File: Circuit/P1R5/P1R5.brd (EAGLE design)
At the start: 50.8 x 50.8 mm, 198 parts, among them J1 2X5_0.05"_CORTEX_DEBUGTH_NOKE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, U1 MK20DX256VLH7, U2 TPS61200, U3 PCA9552BS, U4 PCA9552BS, U5 MPU-9250, U6 25Q40, U7 ESP8266EX, U8 NRF24L01, Y1 8MHz, Y2 34.728kHz, Y3 26 Mhz, Y4 16 Mhz

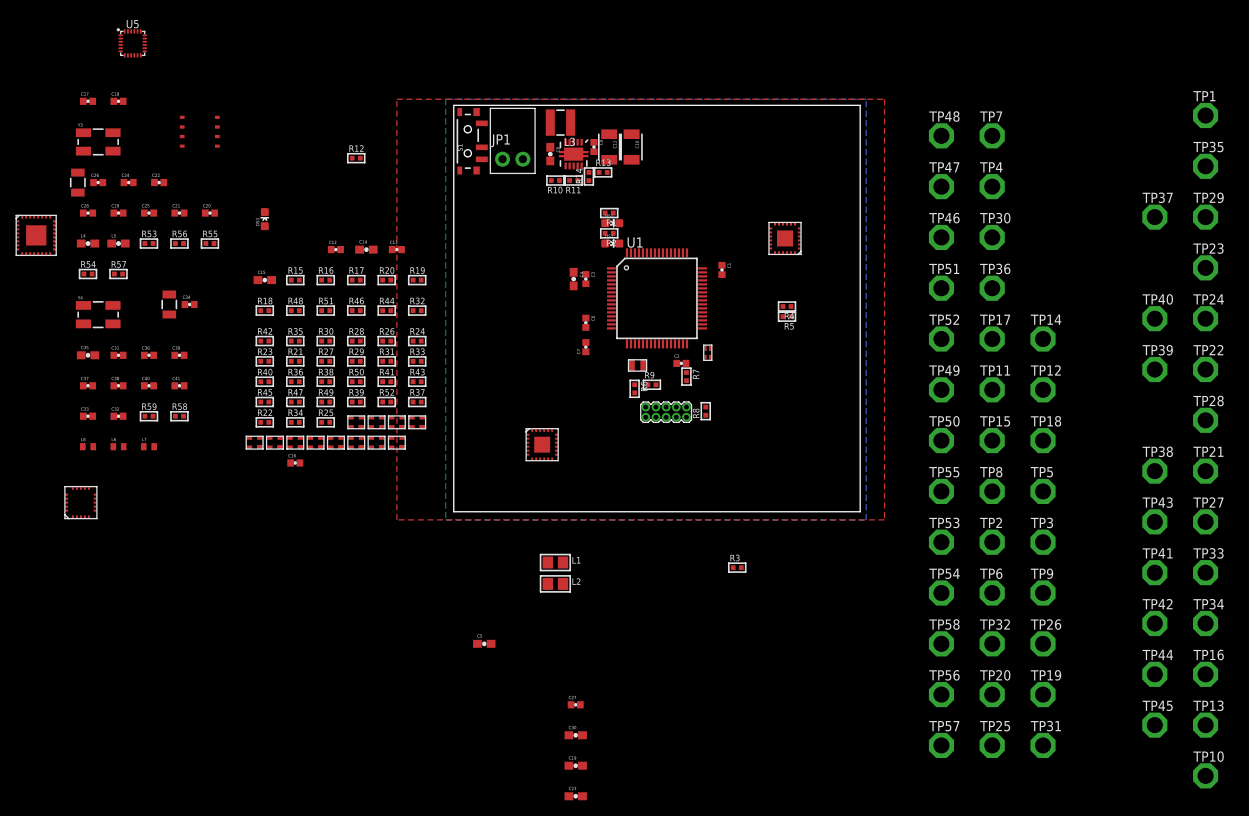
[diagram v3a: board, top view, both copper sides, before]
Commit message: Got majority of PCB layout done.
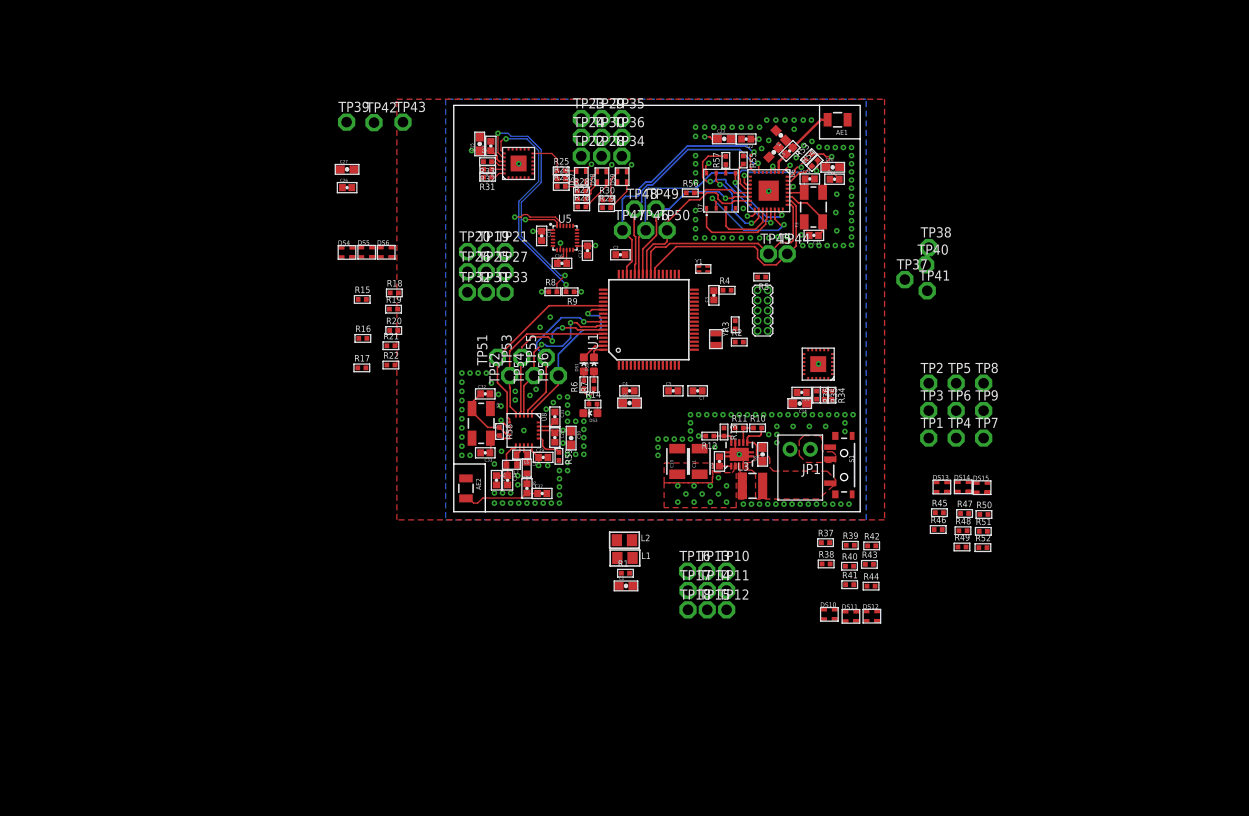
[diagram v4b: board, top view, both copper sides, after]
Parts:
- removed C38: 4.7 pF, SparkFun-Capacitors:0402-CAP
- removed C39: 1.0 pF, SparkFun-Capacitors:0402-CAP
- removed C40, C41: 22 pF, SparkFun-Capacitors:0402-CAP
- removed TP57, TP58: TPPAD1-20, testpad:P1-20
- C1, C6: value 0.1uF -> 10uF; device SparkFun-Capacitors:0402-CAP -> SparkFun-Capacitors:0603-CAP
- C19: value 10uF -> 5.6 pF; device SparkFun-Capacitors:0603-CAP -> SparkFun-Capacitors:0402-CAP
- C20, C27: value 0.1 uF -> 10uF; device SparkFun-Capacitors:0402-CAP -> SparkFun-Capacitors:0603-CAP
- C22: value 15 pF -> 0.1 uF
- C25: value 0.1 uF -> 15 pF
- C26: value 5.6 pF -> 0.1 uF
- C32, C33: value 0.1 uF -> 22 pF
- C34: value 0.1uF -> 2200 pF
- C35: value 10uF -> 4.7 pF; device SparkFun-Capacitors:0603-CAP -> SparkFun-Capacitors:0402-CAP
- C37: value 2200 pF -> 1.0 pF
- C4, C5: value 10uF -> 0.1uF; device SparkFun-Capacitors:0603-CAP -> SparkFun-Capacitors:0402-CAP
- L7: value 3.9 nH -> 2.7 nH
- L8: value 2.7 nH -> 3.9 nH
- R1: value 25 -> 470
- R12: value 25 -> 1.2M
- R13: value 1.2M -> 220K
- R14: value 220K -> 25
- R15, R16, R17, R18, R19, R20: value 10k -> 86.6
- R2: value 25 -> 10k
- R3: value 470 -> 10k
- R31, R32, R33, R34, R35, R36: value 86.6 -> 10k
- R55: value 200 -> 12k
- R56: value 12k -> 10k
- R57: value 10k -> 200
- R58: value 22k -> 1M
- R59: value 1M -> 22k
- R6, R7: value 10k -> 25
- TP1, TP10, TP11, TP12, TP13, TP14, TP15, TP16, TP17, TP18, TP19, TP2, TP20, TP21, TP22, TP23, TP24, TP25, TP26, TP27, TP28, TP29, TP3, TP30, TP31, TP32, TP33, TP34, TP35, TP36, TP37, TP38, TP39, TP4, TP40, TP41, TP42, TP43, TP44, TP45, TP46, TP47, TP48, TP49, TP5, TP50, TP51, TP52, TP53, TP54, TP55, TP56, TP6, TP7, TP8, TP9: value TPPAD1-20 -> TPPAD1-13; device testpad:P1-20 -> testpad:P1-13
- U6: value 25Q40 -> ESP8266EX; device wifi:SOP8 -> wifi:QFN32
- U7: value ESP8266EX -> 25Q40; device wifi:QFN32 -> wifi:SOP8
- moved TP42 116.0 mm to (-9.97, 48.6)
- moved TP43 106.4 mm to (-6.35, 48.7)
- moved TP39 105.7 mm to (-13.4, 48.7)
- moved AE1 95.3 mm to (48.0, 49.0), turned to 90 degrees
- moved TP33 94.3 mm to (6.41, 27.4)
- moved TP34 93.5 mm to (21.0, 44.5)
- moved TP27 93.0 mm to (6.41, 30.0)
- moved R54 91.9 mm to (45.1, 43.6), turned to 45 degrees
- moved TP21 91.8 mm to (6.41, 32.5)
- moved Y3 89.8 mm to (45.0, 38.1), turned to 90 degrees
- moved TP31 89.7 mm to (4.08, 27.4)
- moved TP19 88.9 mm to (4.06, 32.5)
- moved R48 87.9 mm to (63.7, -2.37)
- moved L4 87.7 mm to (40.9, 47.0), turned to 135 degrees
- moved R51 86.7 mm to (66.2, -2.45)
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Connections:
- removed net N$118: C29.2, U7.VDD3P3/4, U7.VDD_RTC/5
- removed net N$61 (its old number): DS7.G, R31.2
- new net N$59: DS13.G, R46.2
- net !CS: now also TP42.TP; no longer TP44.TP
- net !RESET0: now also TP37.TP; no longer TP39.TP
- net !RESET1: now also TP38.TP; no longer TP40.TP
- net 3.3V: now also C17.2, C18.1, C21.2, C22.1, C26.2, C27.1, C28.1, C29.1, C6.1, R12.2, R14.1, R36.2, R53.2, R9.1, U6.1, U6.11, U6.17, U6.29, U6.3, U6.30, U6.4, U7.8; no longer C1.1, C16.2, C17.1, C19.1, C21.1, C25.2, C27.2, C28.2, C32.1, C33.1, C34.1, C35.1, R1.1, R12.1, R13.2, R20.2, R54.2, U6.8, U7.VDD3P3/3, U7.VDDA/1, U7.VDDA/30, U7.VDDD/29, U7.VDDPST/11, U7.VDDPST/17
- net CE: now also TP56.TP; no longer TP58.TP
- net CHIP_EN: now also TP48.TP, U6.7; no longer TP50.TP, U7.CHIP_EN/7
- net CLK: now also R57.1, U7.6; no longer R55.1, U6.6
- net CS: now also U6.20, U7.1; no longer U6.1, U7.SD_CMD/20
- net CSN: now also TP55.TP, U1.57; no longer TP57.TP, U1.49
- net DIO: now also U6.23, U7.5; no longer U6.5, U7.SD_DATA_1/23
- net DO: now also U6.22, U7.2; no longer U6.2, U7.SD_DATA_0/22
- net FSYNC: now also TP39.TP; no longer TP41.TP
- net GND: now also C17.1, C18.2, C21.1, C25.2, C26.1, C27.2, C28.2, C29.2, C6.2, R13.1, R3.1, R31.2, R32.2, R33.2, R34.2, R35.2, R54.2, R55.1, R59.2, U6.PAD, U7.4; no longer C1.2, C17.2, C18.1, C19.2, C21.2, C25.1, C27.1, C28.1, C29.1, C38.2, C39.2, C40.2, C41.2, R14.1, R15.2, R16.2, R17.2, R18.2, R19.2, R53.2, R57.1, R58.2, R9.1, U6.4, U7.GND
- net GPIO0: now also TP50.TP, U6.15; no longer TP52.TP, U7.GPIO0/15
- net GPIO2: now also TP49.TP, U6.14; no longer TP51.TP, U7.GPIO2/14
- net HOLD#: now also U6.18, U7.7; no longer U6.7, U7.SD_DATA_2/18
- net INT: now also TP43.TP; no longer TP45.TP
- net IRQ: now also TP51.TP; no longer TP53.TP
- net MISO: now also TP52.TP, U1.60; no longer TP54.TP, U1.52
- net MOSI: now also TP53.TP, U1.59; no longer TP55.TP, U1.51
- net N$100: now also C24.1, U6.28; no longer C22.1, U7.XTAL_IN/28
- net N$101: now also C19.1; no longer C26.1
- net N$102: now also R55.2, U6.12; no longer R56.2, U7.MTCK/12
- net N$103: now also R56.2, U6.13; no longer R57.2, U7.MTDO/13
- net N$107: now also R54.1, U6.31; no longer R53.1, U7.RES12K/31
- net N$108: now also C32.1, R58.1; no longer C40.1, R59.1
- net N$109: now also C33.1, R58.2; no longer C41.1, R59.2
- net N$11: now also U1.50; no longer U1.58
- net N$111: now also L8.1; no longer L7.1
- net N$112: now also R59.1; no longer R58.1
- net N$114: now also L7.1; no longer L8.1
- net N$115: now also C37.1; no longer C39.1
- net N$116: now also L8.2; no longer L7.2
- net N$117: now also C34.1, C35.1, L7.2; no longer C37.1, C38.1, L8.2
- net N$15: now also U1.49; no longer U1.57
- net N$22: now also C19.2, U6.2; no longer C26.2, U7.LNA/2
- net N$23: now also C25.1, U6.27; no longer C24.1, U7.XTAL_OUT/27
- net N$27: now also R12.1, R13.2; no longer R13.1, R14.2
- net N$28: now also R14.2; no longer R12.2
- net N$29: now also R7.2; no longer R2.2
- net N$3: now also R57.2, U6.21; no longer R55.2, U7.SD_CLK/21
- net N$30: now also R32.1; no longer R16.1
- net N$31: now also R33.1; no longer R17.1
- net N$32: now also R34.1; no longer R18.1
- net N$33: now also R35.1; no longer R19.1
- net N$34: now also R36.1; no longer R20.1
- net N$35: now also R31.1; no longer R15.1
- net N$36: now also DS8.R, R27.2; no longer DS12.R, R44.2
- net N$37: now also DS7.R, R24.2; no longer DS10.R, R39.2
- net N$38: now also DS7.B, R25.2; no longer DS10.B, R40.2
- net N$39: now also DS7.G, R23.2; no longer DS10.G, R37.2
- net N$4: now also C16.2; no longer C18.2
- net N$40: now also DS8.B, R28.2; no longer DS12.B, R46.2
- net N$41: now also DS8.G, R26.2; no longer DS12.G, R42.2
- net N$42: now also DS10.G, R38.2; no longer DS5.G, R25.2
- net N$43: now also DS10.B, R37.2; no longer DS5.B, R22.2
- net N$44: now also DS9.B, R30.2; no longer DS14.B, R51.2
- net N$45: now also DS9.G, R29.2; no longer DS14.G, R48.2
- net N$46: now also R15.1; no longer R21.1
- net N$47: now also DS5.R, R19.2; no longer DS6.R, R28.2
- net N$48: now also R16.1; no longer R23.1
- net N$49: now also R17.1; no longer R24.1
- net N$5: now also U1.52; no longer U1.60
- net N$50: now also DS14.B, R47.2; no longer DS13.B, R43.2
- net N$51: now also R16.2; no longer R23.2
- net N$52: now also DS11.R, R40.2; no longer DS7.R, R29.2
- net N$53: now also R17.2; no longer R24.2
- net N$54: now also R15.2; no longer R21.2
- net N$55: now also DS5.B, R20.2; no longer DS6.B, R30.2
- net N$56: now also DS5.G, R18.2; no longer DS6.G, R26.2
- net N$58: now also DS12.B, R42.2; no longer DS9.B, R33.2
- net N$6: now also U1.51; no longer U1.59
- net N$60: now also R18.1; no longer R26.1
- net N$62: now also DS14.G, R49.2; no longer DS13.G, R47.2
- net N$63: now also DS11.B, R39.2; no longer DS7.B, R27.2
- net N$64: now also DS12.G, R44.2; no longer DS9.G, R36.2
- net N$65: now also DS6.B, R22.2; no longer DS8.B, R35.2
- net N$66: now also DS6.G, R21.2; no longer DS8.G, R32.2
- net N$67: now also DS14.R, R48.2; no longer DS13.R, R45.2
- net N$68: now also DS13.B, R45.2; no longer DS11.B, R38.2
- net N$69: now also R19.1; no longer R28.1
- net N$7: now also R6.2; no longer R1.2
- net N$70: now also R50.2; no longer R49.2
- net N$71: now also R20.1; no longer R30.1
- net N$72: now also R21.1; no longer R32.1
- net N$73: now also R22.1; no longer R35.1
- net N$74: now also R23.1; no longer R37.1
- net N$75: now also R24.1; no longer R39.1
- net N$76: now also R25.1; no longer R40.1
- net N$77: now also R26.1; no longer R42.1
- net N$78: now also R27.1; no longer R44.1
- net N$79: now also R28.1; no longer R46.1
- net N$80: now also R29.1; no longer R48.1
- net N$81: now also R30.1; no longer R51.1
- net N$82: now also DS12.R, R43.2; no longer DS9.R, R34.2
- net N$83: now also R51.2; no longer R50.2
- net N$84: now also R37.1; no longer R22.1
- net N$85: now also R38.1; no longer R25.1
- net N$86: now also R39.1; no longer R27.1
- net N$87: now also R40.1; no longer R29.1
- net N$88: now also R41.1; no longer R31.1
- net N$89: now also R42.1; no longer R33.1
- net N$90: now also R43.1; no longer R34.1
- net N$91: now also R44.1; no longer R36.1
- net N$92: now also R45.1; no longer R38.1
- net N$93: now also R46.1; no longer R41.1
- net N$94: now also R47.1; no longer R43.1
- net N$95: now also R48.1; no longer R45.1
- net N$96: now also R49.1; no longer R47.1
- net N$97: now also R50.1; no longer R49.1
- net N$98: now also R51.1; no longer R50.1
- net PTA0: now also R3.2; no longer R9.2
- net PTA1: now also R4.2; no longer R7.2
- net PTA3: now also R2.2; no longer R6.2
- net RESET_B: now also R5.2; no longer R8.2
- net SCK: now also TP54.TP, U1.58; no longer TP56.TP, U1.50
- net SCL: now also R9.2, TP40.TP; no longer R5.2, TP42.TP
- net SDA: now also R8.2, TP41.TP; no longer R4.2, TP37.TP, TP38.TP, TP43.TP
- net U0RX: now also TP45.TP, U6.25; no longer TP47.TP, U7.U0RXD/25
- net U0TX: now also TP44.TP, U6.26; no longer TP46.TP, U7.U0TXD/26
- net VDDA: now also C1.1, R1.1; no longer C5.1, R3.1
- net VREFH: now also C5.1, R1.2; no longer C6.1, R3.2
- net VREFL: now also C1.2; no longer C6.2
- net WIFI_RESET: now also R53.1, TP46.TP, U6.32; no longer R54.1, TP48.TP, U7.EXT_RSTB/32
- net WP#: now also U6.19, U7.3; no longer U6.3, U7.SD_DATA_3/19
- net XPD_DCDC: now also TP47.TP, U6.8; no longer TP49.TP, U7.XPD_DCDC/8
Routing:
- net 3.3V: track 0.00 -> 47.5 mm, vias 0 -> 35
- net SDA: track 0.00 -> 36.6 mm, vias 0 -> 3
- net WIFI_RESET: track 0.00 -> 35.7 mm, vias 0 -> 1
- net SCL: track 0.00 -> 35.4 mm, vias 0 -> 3
- net XPD_DCDC: track 0.00 -> 33.1 mm, vias 0 -> 1
- net CHIP_EN: track 0.00 -> 29.5 mm, vias 0 -> 1
- net U0TX: track 0.00 -> 28.5 mm
- net U0RX: track 0.00 -> 27.3 mm
- net IRQ: track 0.00 -> 24.7 mm
- net GPIO2: track 0.00 -> 22.0 mm, vias 0 -> 1
- net GPIO0: track 0.00 -> 21.3 mm
- net CE: track 0.00 -> 21.1 mm, vias 0 -> 1
- net MISO: track 0.00 -> 21.0 mm
- net MOSI: track 0.00 -> 21.0 mm, vias 0 -> 2
- net CSN: track 0.00 -> 20.5 mm, vias 0 -> 1
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- added copper zone on layer 1, net 3.3V
- added copper zone on layer 1, net N$104
- added copper zone on layer 1, net N$24
- added copper zone on layer 1, net V_IN
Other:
- outline, holes or cut-outs redrawn

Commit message: More work on PCB.
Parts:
- removed C15: 10uF, SparkFun-Capacitors:0603-CAP
- removed C16: 0.1 uF, SparkFun-Capacitors:0402-CAP
- removed C37: 1.0 pF, SparkFun-Capacitors:0402-CAP
- removed R30: 86.6, appfruits:_0402
- removed R31, R32, R33, R34, R35: 10k, appfruits:_0402
- removed R59: 22k, appfruits:_0402
- C10: value 22uF -> 0.1uF; device SparkFun-Capacitors:1210 -> SparkFun-Capacitors:0402-CAP
- C12: value 0.1uF -> 22uF; device SparkFun-Capacitors:0402-CAP -> SparkFun-Capacitors:1210
- C14, C6, C8: value 10uF -> 0.1uF; device SparkFun-Capacitors:0603-CAP -> SparkFun-Capacitors:0402-CAP
- C19: value 5.6 pF -> 0.1 uF
- C20: value 10uF -> 5.6 pF; device SparkFun-Capacitors:0603-CAP -> SparkFun-Capacitors:0402-CAP
- C21, C29: value 0.1 uF -> 10uF; device SparkFun-Capacitors:0402-CAP -> SparkFun-Capacitors:0603-CAP
- C23, C27: value 10uF -> 0.1 uF; device SparkFun-Capacitors:0603-CAP -> SparkFun-Capacitors:0402-CAP
- C24: value 15 pF -> 10uF; device SparkFun-Capacitors:0402-CAP -> SparkFun-Capacitors:0603-CAP
- C26: value 0.1 uF -> 15 pF
- C30: value 10uF -> .033 uF; device SparkFun-Capacitors:0603-CAP -> SparkFun-Capacitors:0402-CAP
- C31: value .033 uF -> 22 pF
- C33: value 22 pF -> 2200 pF
- C34: value 2200 pF -> 4.7 pF
- C35: value 4.7 pF -> 1.5 pF
- C36: value 1.5 pF -> 1.0 pF
- C4, C7, C9: value 0.1uF -> 10uF; device SparkFun-Capacitors:0402-CAP -> SparkFun-Capacitors:0603-CAP
- R1: value 470 -> 10k
- R10: value 2M -> 220K
- R11: value 220K -> 1.2M
- R12: value 1.2M -> 220K
- R13: value 220K -> 25
- R14: value 25 -> 86.6
- R36: value 10k -> 86.6
- R5: value 10k -> 25
- R52: value 86.6 -> 12k
- R55: value 12k -> 10k
- R56: value 10k -> 200
- R57: value 200 -> 1M
- R58: value 1M -> 22k
- R7: value 25 -> 10k
- R9: value 10k -> 2M
- TP37, TP38, TP39, TP40, TP42, TP43, TP44, TP45, TP46, TP47, TP48, TP49, TP50, TP51, TP52, TP53, TP54, TP55, TP56: value TPPAD1-13 -> TPTP08R; device testpad:P1-13 -> testpad:TP08R
- moved TP41 65.1 mm to (-4.70, 40.4)
- moved TP6 63.9 mm to (1.65, 31.1)
- moved TP4 63.4 mm to (1.65, 26.0)
- moved TP5 62.4 mm to (1.65, 28.5)
- moved TP15 62.3 mm to (21.0, 49.1)
- moved TP9 62.3 mm to (6.73, 31.1)
- moved TP7 61.8 mm to (6.73, 26.0)
- moved TP8 60.8 mm to (6.73, 28.5)
- moved TP14 60.5 mm to (18.5, 49.1)
- moved TP18 59.6 mm to (21.0, 46.8)
- moved TP38 59.2 mm to (1.63, 45.9)
- moved TP13 58.7 mm to (15.9, 49.1)
- moved C26 58.6 mm to (45.0, 34.5), turned to 180 degrees
- moved TP12 58.2 mm to (21.0, 44.5)
- moved TP3 58.2 mm to (4.19, 31.1)
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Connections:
- removed net N$30: R32.1, U3.23
- removed net N$31: R33.1, U3.22
- removed net N$32: R34.1, U4.24
- removed net N$33: R35.1, U4.23
- removed net N$34: R36.1, U4.22
- removed net N$35: R31.1, U3.24
- removed net VREFH: C5.1, R1.2, U1.14
- removed net VREFL: C1.2, C5.2, C7.2, L2.2, U1.15, U1.16
- new net AGND: C4.2, C6.2, C8.2, L2.2, U1.15, U1.16
- net !RESET0: now also TP39.TP; no longer TP37.TP
- net !RESET1: now also TP40.TP; no longer TP38.TP
- net 3.3V: now also C1.1, C18.2, C19.1, C21.1, C22.2, C24.1, C5.1, C7.1, R1.1, R11.2, R13.1, R3.1, R52.2, TP1.TP, TP16.TP, TP17.TP, TP2.TP, TP32.TP, TP33.TP, TP34.TP, TP35.TP, U4.22; no longer C10.1, C15.1, C17.2, C18.1, C20.1, C21.2, C22.1, C26.2, C30.1, C4.1, C6.1, R12.2, R14.1, R2.1, R36.2, R53.2, R9.1, TP12.TP, TP15.TP, TP19.TP, TP24.TP, TP25.TP, TP30.TP, TP6.TP, TP9.TP
- net CHIP_EN: now also TP46.TP; no longer TP48.TP
- net CLK: now also R56.1; no longer R57.1
- net FSYNC: now also TP41.TP; no longer TP39.TP
- net GND: now also C1.2, C18.1, C19.2, C21.2, C22.1, C26.2, C30.1, C31.2, C36.2, C5.2, C7.2, R10.1, R12.1, R2.1, R53.2, R54.1, R58.2, TP13.TP, TP15.TP, TP25.TP, TP27.TP, TP28.TP, TP30.TP, TP4.TP, TP6.TP, U3.22, U3.23, U3.24, U4.23, U4.24; no longer C15.2, C16.1, C18.2, C20.2, C21.1, C22.2, C26.1, C30.2, C31.1, C35.2, C37.2, C4.2, C6.2, C8.2, R11.1, R13.1, R3.1, R31.2, R32.2, R33.2, R34.2, R35.2, R54.2, R56.1, R59.2, TP11.TP, TP17.TP, TP2.TP, TP20.TP, TP23.TP, TP32.TP, TP35.TP, TP8.TP
- net GPIO0: now also TP49.TP; no longer TP50.TP
- net GPIO2: now also TP47.TP; no longer TP49.TP
- net N$100: now also C25.1; no longer C24.1
- net N$101: now also C20.1; no longer C19.1
- net N$102: now also R54.2; no longer R55.2
- net N$103: now also R55.2; no longer R56.2
- net N$107: now also R53.1; no longer R54.1
- net N$108: now also C31.1, R57.1; no longer C32.1, R58.1
- net N$109: now also C32.1, R57.2; no longer C33.1, R58.2
- net N$11: now also TP9.TP; no longer TP33.TP
- net N$112: now also R58.1; no longer R59.1
- net N$113: now also C30.2; no longer C31.2
- net N$115: now also C35.2, C36.1; no longer C36.2, C37.1
- net N$116: now also C35.1; no longer C36.1
- net N$117: now also C33.1; no longer C35.1
- net N$12: now also TP10.TP; no longer TP22.TP
- net N$14: now also TP11.TP; no longer TP28.TP
- net N$15: now also TP12.TP; no longer TP34.TP
- net N$16: now also TP24.TP; no longer TP16.TP
- net N$17: now also TP21.TP; no longer TP7.TP
- net N$18: now also TP22.TP; no longer TP10.TP
- net N$19: now also TP23.TP; no longer TP13.TP
- net N$20: now also TP20.TP; no longer TP4.TP
- net N$21: now also TP19.TP; no longer TP1.TP
- net N$22: now also C20.2; no longer C19.2
- net N$23: now also C26.1; no longer C25.1
- net N$25: now also C10.1; no longer C9.1
- net N$26: now also R10.2, R9.1; no longer R10.1, R11.2
- net N$27: now also R11.1, R12.2; no longer R12.1, R13.2
- net N$28: now also R13.2; no longer R14.2
- net N$29: now also R6.2; no longer R7.2
- net N$3: now also R56.2; no longer R57.2
- net N$36: now also R26.2; no longer R27.2
- net N$37: now also R23.2; no longer R24.2
- net N$38: now also R24.2; no longer R25.2
- net N$39: now also R22.2; no longer R23.2
- net N$4: now also C17.2; no longer C16.2
- net N$40: now also R27.2; no longer R28.2
- net N$41: now also R25.2; no longer R26.2
- net N$42: now also R37.2; no longer R38.2
- net N$43: now also R36.2; no longer R37.2
- net N$44: now also R29.2; no longer R30.2
- net N$45: now also R28.2; no longer R29.2
- net N$46: now also R14.1; no longer R15.1
- net N$47: now also R18.2; no longer R19.2
- net N$48: now also R15.1; no longer R16.1
- net N$49: now also R16.1; no longer R17.1
- net N$5: now also TP7.TP; no longer TP21.TP
- net N$50: now also R46.2; no longer R47.2
- net N$51: now also R15.2; no longer R16.2
- net N$52: now also R39.2; no longer R40.2
- net N$53: now also R16.2; no longer R17.2
- net N$54: now also R14.2; no longer R15.2
- net N$55: now also R19.2; no longer R20.2
- net N$56: now also R17.2; no longer R18.2
- net N$57: now also R51.2; no longer R52.2
- net N$58: now also R41.2; no longer R42.2
- net N$59: now also R45.2; no longer R46.2
- net N$6: now also TP8.TP; no longer TP27.TP
- net N$60: now also R17.1; no longer R18.1
- net N$61: now also R40.2; no longer R41.2
- net N$62: now also R48.2; no longer R49.2
- net N$63: now also R38.2; no longer R39.2
- net N$64: now also R43.2; no longer R44.2
- net N$65: now also R21.2; no longer R22.2
- net N$66: now also R20.2; no longer R21.2
- net N$67: now also R47.2; no longer R48.2
- net N$68: now also R44.2; no longer R45.2
- net N$69: now also R18.1; no longer R19.1
- net N$7: now also R5.2; no longer R6.2
- net N$70: now also R49.2; no longer R50.2
- net N$71: now also R19.1; no longer R20.1
- net N$72: now also R20.1; no longer R21.1
- net N$73: now also R21.1; no longer R22.1
- net N$74: now also R22.1; no longer R23.1
- net N$75: now also R23.1; no longer R24.1
- net N$76: now also R24.1; no longer R25.1
- net N$77: now also R25.1; no longer R26.1
- net N$78: now also R26.1; no longer R27.1
- net N$79: now also R27.1; no longer R28.1
- net N$80: now also R28.1; no longer R29.1
- net N$81: now also R29.1; no longer R30.1
- net N$82: now also R42.2; no longer R43.2
- net N$83: now also R50.2; no longer R51.2
- net N$84: now also R36.1; no longer R37.1
- net N$85: now also R37.1; no longer R38.1
- net N$86: now also R38.1; no longer R39.1
- net N$87: now also R39.1; no longer R40.1
- net N$88: now also R40.1; no longer R41.1
- net N$89: now also R41.1; no longer R42.1
- net N$90: now also R42.1; no longer R43.1
- net N$91: now also R43.1; no longer R44.1
- net N$92: now also R44.1; no longer R45.1
- net N$93: now also R45.1; no longer R46.1
- net N$94: now also R46.1; no longer R47.1
- net N$95: now also R47.1; no longer R48.1
- net N$96: now also R48.1; no longer R49.1
- net N$97: now also R49.1; no longer R50.1
- net N$98: now also R50.1; no longer R51.1
- net N$99: now also R51.1; no longer R52.1
- net PTA0: now also R2.2; no longer R3.2
- net PTA1: now also R3.2; no longer R4.2
- net PTA3: now also R1.2; no longer R2.2
- net RESET_B: now also R4.2; no longer R5.2
- net SCL: now also R8.2, TP38.TP; no longer R9.2, TP40.TP
- net SDA: now also R7.2, TP37.TP; no longer R8.2, TP41.TP
- net U0RX: now also TP50.TP; no longer TP45.TP
- net U0TX: now also TP48.TP; no longer TP44.TP
- net VDDA: now also C4.1, C6.1, U1.14; no longer C1.1, R1.1
- net VREF_OUT: now also C8.1; no longer C7.1
- net V_IN: now also C9.1, R9.2; no longer C8.1, R10.2
- net WIFI_RESET: now also R52.1, TP45.TP; no longer R53.1, TP46.TP
- net XPD_DCDC: now also TP44.TP; no longer TP47.TP
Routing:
- net 3.3V: track 47.5 -> 66.6 mm, vias 35 -> 43
- net RESET_B: track 0.00 -> 14.9 mm
- net PTA3: track 0.00 -> 10.3 mm, vias 0 -> 1
- net PTA1: track 0.00 -> 9.20 mm
- net PTA2: track 0.00 -> 8.47 mm, vias 0 -> 1
- net PTA0: track 0.00 -> 8.37 mm
- net SCL: track 35.4 -> 42.6 mm, vias 3 -> 4
- net SDA: track 36.6 -> 42.5 mm
- net N$73: track 0.00 -> 5.00 mm
- net N$76: track 4.79 -> 0.00 mm
- net N$41: track 4.16 -> 0.00 mm
- net N$1: track 0.00 -> 4.09 mm
- net N$2: track 0.00 -> 4.08 mm
- net N$45: track 4.03 -> 0.00 mm
- net N$44: track 3.91 -> 0.00 mm
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- added copper zone on layer 1, net AGND
- added copper zone on layer 1, net VDDA
